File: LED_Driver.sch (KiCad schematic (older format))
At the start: 0 parts

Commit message: Overall Schematic
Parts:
- added C? (x2): C, ~, symbol C
- added D?: DIODESCH, ~, symbol DIODESCH
- added L?: INDUCTOR, ~, symbol INDUCTOR
- added R?: R, ~, symbol R
- added U?: AP5726, symbol AP5726
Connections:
- new net: D?.1 (A), L?.2, U?.1 (SW)
- new net +5V: C?.1, L?.1, U?.6 (VIN)
- new net GND: C?.2, C?.2, R?.2, U?.2 (GND)
- new net LED_EN_PWM: U?.4 (EN)
- new net LED_STRING+: C?.1, D?.2 (K), U?.5 (OVP)
- new net LED_STRING-: R?.1, U?.3 (FB)
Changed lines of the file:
@@
 $Descr A4 11693 8268
 encoding utf-8
-Sheet 6 9
+Sheet 5 9
 Title ""
-Date "22 sep 2013"
+Date "28 sep 2013"
 Rev ""
 Comp ""
@@
 Comment4 ""
 $EndDescr
-Text HLabel 8450 2900 2    60   Input ~ 0
-EN
-Text HLabel 8450 3050 2    60   Input ~ 0
-FREQ
-Text HLabel 9300 2900 2    60   Output ~ 0
-String+
-Text HLabel 9300 3050 2    60   Input ~ 0
-String-
+Text HLabel 4850 3700 0    60   Input ~ 0
+LED_EN_PWM
+Text HLabel 9550 2400 2    60   Output ~ 0
+LED_STRING+
+Text HLabel 9550 3850 2    60   Input ~ 0
+LED_STRING-
+$Comp
+L AP5726 U?
+U 1 1 52469A62
+P 6050 4200
+F 0 "U?" H 6400 4050 60  0000 C CNN
+F 1 "AP5726" H 6050 4750 60  0000 C CNN
+F 2 "" H 6050 4200 60  0000 C CNN
+F 3 "" H 6050 4200 60  0000 C CNN
+	1    6050 4200
+	1    0    0    -1
+$EndComp
+$Comp
+L +5V #PWR?
+U 1 1 52469C96
+P 5050 2400
+F 0 "#PWR?" H 5050 2490 20  0001 C CNN
+F 1 "+5V" H 5050 2490 30  0000 C CNN
+F 2 "" H 5050 2400 60  0000 C CNN
+F 3 "" H 5050 2400 60  0000 C CNN
+	1    5050 2400
+	1    0    0    -1
+$EndComp
+$Comp
+L GND #PWR?
+U 1 1 52469CA5
+P 5350 2950
+F 0 "#PWR?" H 5350 2950 30  0001 C CNN
+F 1 "GND" H 5350 2880 30  0001 C CNN
+F 2 "" H 5350 2950 60  0000 C CNN
+F 3 "" H 5350 2950 60  0000 C CNN
+	1    5350 2950
+	1    0    0    -1
+$EndComp
+$Comp
+L C C?
+U 1 1 52469CBE
+P 5350 2650
+F 0 "C?" H 5350 2750 40  0000 L CNN
+F 1 "C" H 5356 2565 40  0000 L CNN
+F 2 "~" H 5388 2500 30  0000 C CNN
+F 3 "~" H 5350 2650 60  0000 C CNN
+	1    5350 2650
+	1    0    0    -1
+$EndComp
+$Comp
+L INDUCTOR L?
+U 1 1 52469CCD
+P 6100 2400
+F 0 "L?" V 6050 2400 40  0000 C CNN
+F 1 "INDUCTOR" V 6200 2400 40  0000 C CNN
+F 2 "~" H 6100 2400 60  0000 C CNN
+F 3 "~" H 6100 2400 60  0000 C CNN
+	1    6100 2400
+	0    -1   -1   0
+$EndComp
+Wire Wire Line
+	5350 2950 5350 2850
+Wire Wire Line
+	5050 2400 5800 2400
+Wire Wire Line
+	5850 2850 5850 2550
+Wire Wire Line
+	5850 2550 5750 2550
+Wire Wire Line
+	5750 2550 5750 2400
+Connection ~ 5750 2400
+Wire Wire Line
+	6350 2850 6350 2550
+Wire Wire Line
+	6350 2550 6450 2550
+Wire Wire Line
+	6450 2550 6450 2400
+Wire Wire Line
+	6400 2400 6500 2400
+$Comp
+L DIODESCH D?
+U 1 1 52469D25
+P 6700 2400
+F 0 "D?" H 6700 2500 40  0000 C CNN
+F 1 "DIODESCH" H 6700 2300 40  0000 C CNN
+F 2 "~" H 6700 2400 60  0000 C CNN
+F 3 "~" H 6700 2400 60  0000 C CNN
+	1    6700 2400
+	1    0    0    -1
+$EndComp
+Connection ~ 6450 2400
+Wire Wire Line
+	6900 2400 9550 2400
+Wire Wire Line
+	5350 2450 5350 2400
+Connection ~ 5350 2400
+$Comp
+L C C?
+U 1 1 52469D70
+P 9000 2600
+F 0 "C?" H 9000 2700 40  0000 L CNN
+F 1 "C" H 9006 2515 40  0000 L CNN
+F 2 "~" H 9038 2450 30  0000 C CNN
+F 3 "~" H 9000 2600 60  0000 C CNN
+	1    9000 2600
+	1    0    0    -1
+$EndComp
+Wire Wire Line
+	6000 4500 6000 4550
+$Comp
+L GND #PWR?
+U 1 1 52469D8F
+P 7100 4700
+F 0 "#PWR?" H 7100 4700 30  0001 C CNN
+F 1 "GND" H 7100 4630 30  0001 C CNN
+F 2 "" H 7100 4700 60  0000 C CNN
+F 3 "" H 7100 4700 60  0000 C CNN
+	1    7100 4700
+	1    0    0    -1
+$EndComp
+Wire Wire Line
+	6950 2400 6950 3500
+Wire Wire Line
+	6950 3500 6800 3500
+Connection ~ 6950 2400
+Wire Wire Line
+	4850 3700 5350 3700
+$Comp
+L R R?
+U 1 1 52469E2F
+P 7100 4150
+F 0 "R?" V 7180 4150 40  0000 C CNN
+F 1 "R" V 7107 4151 40  0000 C CNN
+F 2 "~" V 7030 4150 30  0000 C CNN
+F 3 "~" H 7100 4150 30  0000 C CNN
+	1    7100 4150
+	1    0    0    -1
+$EndComp
+Wire Wire Line
+	6800 3850 9550 3850
+Wire Wire Line
+	7100 3850 7100 3900
+Wire Wire Line
+	7100 4400 7100 4700
+Connection ~ 9000 2400
+$Comp
+L GND #PWR?
+U 1 1 5246A0FA
+P 9000 2900
+F 0 "#PWR?" H 9000 2900 30  0001 C CNN
+F 1 "GND" H 9000 2830 30  0001 C CNN
+F 2 "" H 9000 2900 60  0000 C CNN
+F 3 "" H 9000 2900 60  0000 C CNN
+	1    9000 2900
+	1    0    0    -1
+$EndComp
+Wire Wire Line
+	9000 2800 9000 2900
+Wire Wire Line
+	6000 4550 7100 4550
+Connection ~ 7100 4550
+Connection ~ 7100 3850
 $EndSCHEMATC

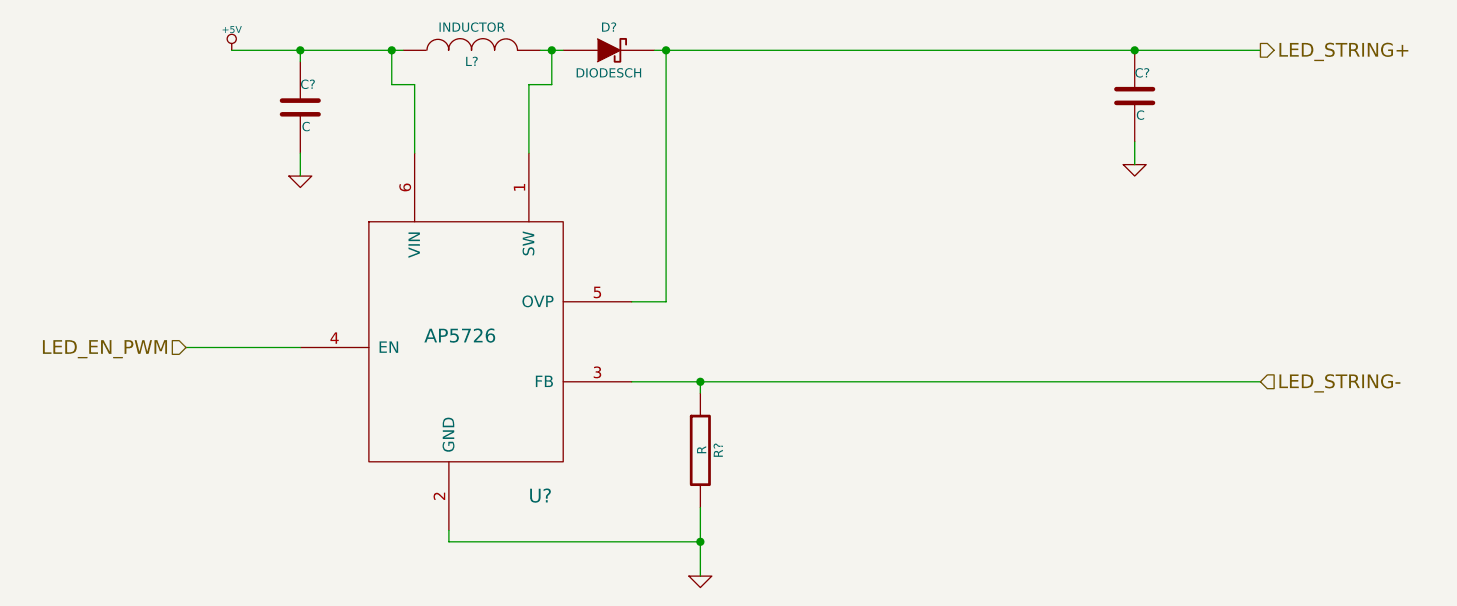
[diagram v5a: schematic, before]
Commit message: Preliminary Module Layouts
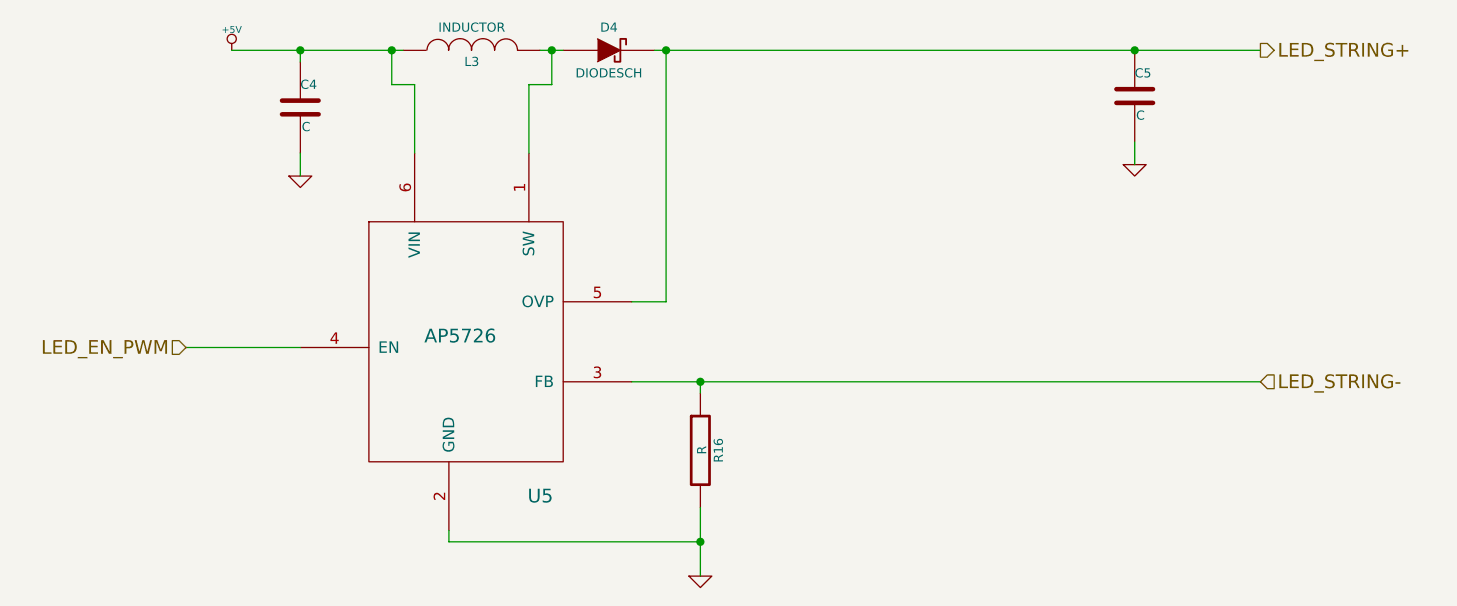
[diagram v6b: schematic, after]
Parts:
- gave numbers to parts that had none: 6
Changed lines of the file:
@@
 $Descr A4 11693 8268
 encoding utf-8
-Sheet 5 9
+Sheet 4 9
 Title ""
-Date "30 sep 2013"
+Date "15 oct 2013"
 Rev ""
 Comp ""
@@
 LED_STRING-
 $Comp
-L AP5726 U?
+L AP5726 U5
 U 1 1 52469A62
 P 6050 4200
-F 0 "U?" H 6400 4050 60  0000 C CNN
+F 0 "U5" H 6400 4050 60  0000 C CNN
 F 1 "AP5726" H 6050 4750 60  0000 C CNN
 F 2 "" H 6050 4200 60  0000 C CNN
@@
 $EndComp
 $Comp
-L +5V #PWR?
+L +5V #PWR032
 U 1 1 52469C96
 P 5050 2400
-F 0 "#PWR?" H 5050 2490 20  0001 C CNN
+F 0 "#PWR032" H 5050 2490 20  0001 C CNN
 F 1 "+5V" H 5050 2490 30  0000 C CNN
 F 2 "" H 5050 2400 60  0000 C CNN
@@
 $EndComp
 $Comp
-L GND #PWR?
+L GND #PWR033
 U 1 1 52469CA5
 P 5350 2950
-F 0 "#PWR?" H 5350 2950 30  0001 C CNN
+F 0 "#PWR033" H 5350 2950 30  0001 C CNN
 F 1 "GND" H 5350 2880 30  0001 C CNN
 F 2 "" H 5350 2950 60  0000 C CNN
@@
 $EndComp
 $Comp
-L C C?
+L C C4
 U 1 1 52469CBE
 P 5350 2650
-F 0 "C?" H 5350 2750 40  0000 L CNN
+F 0 "C4" H 5350 2750 40  0000 L CNN
 F 1 "C" H 5356 2565 40  0000 L CNN
 F 2 "~" H 5388 2500 30  0000 C CNN
@@
 $EndComp
 $Comp
-L INDUCTOR L?
+L INDUCTOR L3
 U 1 1 52469CCD
 P 6100 2400
-F 0 "L?" V 6050 2400 40  0000 C CNN
+F 0 "L3" V 6050 2400 40  0000 C CNN
 F 1 "INDUCTOR" V 6200 2400 40  0000 C CNN
 F 2 "~" H 6100 2400 60  0000 C CNN
@@
 	6400 2400 6500 2400
 $Comp
-L DIODESCH D?
+L DIODESCH D4
 U 1 1 52469D25
 P 6700 2400
-F 0 "D?" H 6700 2500 40  0000 C CNN
+F 0 "D4" H 6700 2500 40  0000 C CNN
 F 1 "DIODESCH" H 6700 2300 40  0000 C CNN
 F 2 "~" H 6700 2400 60  0000 C CNN
@@
 Connection ~ 5350 2400
 $Comp
-L C C?
+L C C5
 U 1 1 52469D70
 P 9000 2600
-F 0 "C?" H 9000 2700 40  0000 L CNN
+F 0 "C5" H 9000 2700 40  0000 L CNN
 F 1 "C" H 9006 2515 40  0000 L CNN
 F 2 "~" H 9038 2450 30  0000 C CNN
@@
 	6000 4500 6000 4550
 $Comp
-L GND #PWR?
+L GND #PWR034
 U 1 1 52469D8F
 P 7100 4700
-F 0 "#PWR?" H 7100 4700 30  0001 C CNN
+F 0 "#PWR034" H 7100 4700 30  0001 C CNN
 F 1 "GND" H 7100 4630 30  0001 C CNN
 F 2 "" H 7100 4700 60  0000 C CNN
@@
 	4850 3700 5350 3700
 $Comp
-L R R?
+L R R16
 U 1 1 52469E2F
 P 7100 4150
-F 0 "R?" V 7180 4150 40  0000 C CNN
+F 0 "R16" V 7180 4150 40  0000 C CNN
 F 1 "R" V 7107 4151 40  0000 C CNN
 F 2 "~" V 7030 4150 30  0000 C CNN
@@
 Connection ~ 9000 2400
 $Comp
-L GND #PWR?
+L GND #PWR035
 U 1 1 5246A0FA
 P 9000 2900
-F 0 "#PWR?" H 9000 2900 30  0001 C CNN
+F 0 "#PWR035" H 9000 2900 30  0001 C CNN
 F 1 "GND" H 9000 2830 30  0001 C CNN
 F 2 "" H 9000 2900 60  0000 C CNN
